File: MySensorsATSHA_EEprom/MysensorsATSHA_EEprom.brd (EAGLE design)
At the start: 19.5 x 12.1 mm, 4 parts

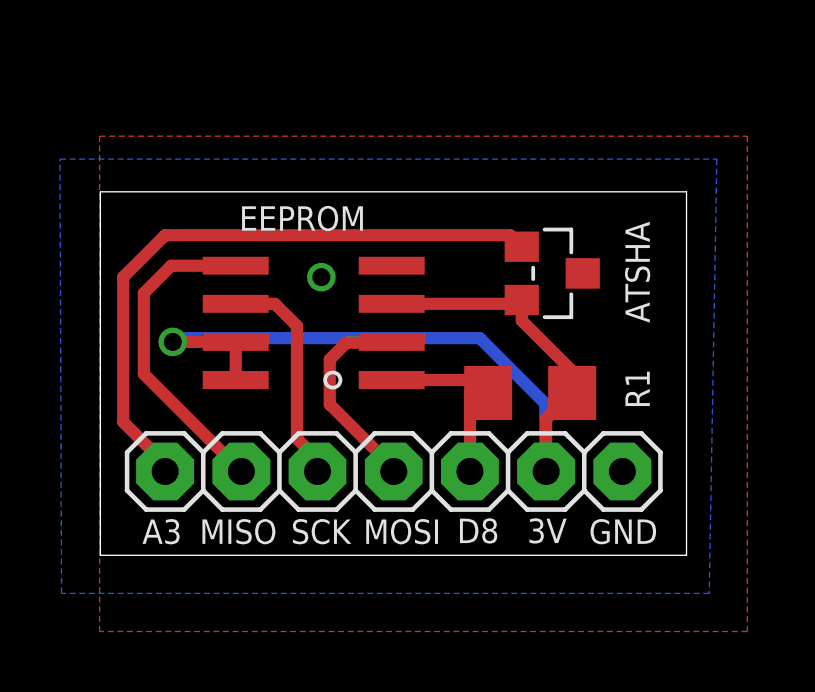
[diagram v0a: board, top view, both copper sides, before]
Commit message: silkscreen updated, bom added
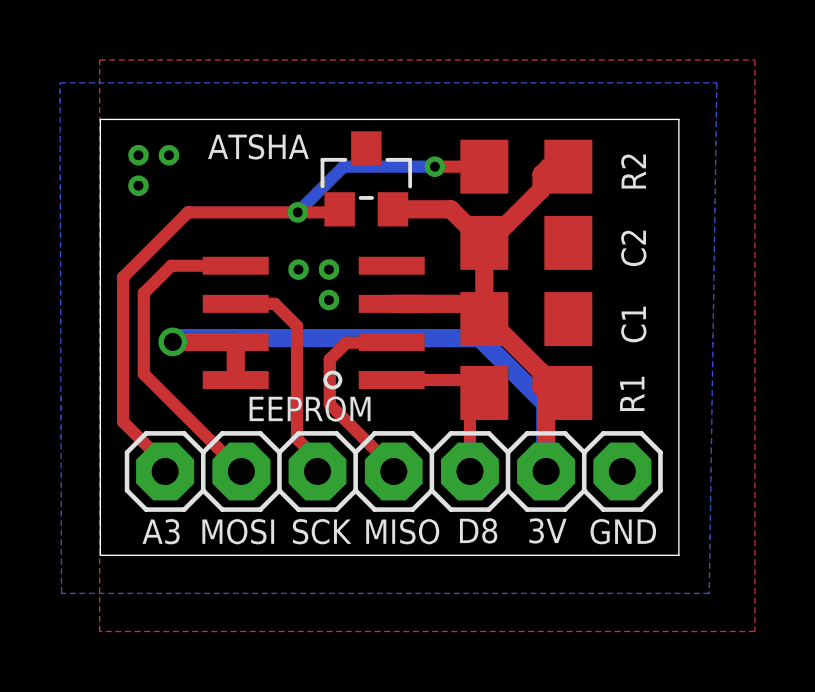
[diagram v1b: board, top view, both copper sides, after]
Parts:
- added C1, C2: 100n, LowPowerLab:1206
- added R2: 4k7, SparkFun-Resistors:1206
- R1: value (none) -> 56k
- moved ATSHA 6.95 mm to (8.89, 12.5), turned to 0 degrees
- moved R1 0.13 mm to (14.2, 5.41)
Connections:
- net A3: now also R2.1
- net GND: now also C1.1, C2.1
- net VCC: now also C1.2, C2.2, R2.2
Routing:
- net VCC: track 30.2 -> 39.6 mm
- net A3: track 21.1 -> 22.1 mm, vias 0 -> 2
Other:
- board size 19.5 x 12.1 mm -> 19.3 x 14.5 mm
